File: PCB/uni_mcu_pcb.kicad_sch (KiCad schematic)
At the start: 1 part

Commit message: Добавлены некоторые компоненты на плату
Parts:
- added J?: USB_C_Receptacle_USB2.0, symbol Connector:USB_C_Receptacle_USB2.0
- added U?: CA56-12EWA, Display_7Segment:CA56-12EWA, symbol Display_Character:CA56-12EWA
- added U?: USBLC6-2P6, Package_TO_SOT_SMD:SOT-666, symbol Power_Protection:USBLC6-2P6
- added U?: CH330N, Package_SO:SOIC-8_3.9x4.9mm_P1.27mm, symbol Interface_USB:CH330N
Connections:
- new net: J?.A1 (GND), J?.A12 (GND), J?.B1 (GND), J?.B12 (GND)
- new net: J?.A4 (VBUS), J?.A9 (VBUS), J?.B4 (VBUS), J?.B9 (VBUS)
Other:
- moved on the sheet: U?
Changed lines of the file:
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@@
 (kicad_sch (version 20211123) (generator eeschema)
   (paper "A4")
-  (symbol (lib_id "MCU_ST_STM32F0:STM32F030C8Tx") (at 113.03 88.9 0) (unit 1)
+  (symbol (lib_id "Connector:USB_C_Receptacle_USB2.0") (at 29.845 62.23 0) (unit 1)
     (in_bom yes) (on_board yes) (fields_autoplaced)
-    (property "Reference" "U?" (id 0) (at 117.5894 129.0304 0)
+    (property "Reference" "J?" (id 0) (at 29.845 40.7502 0))
+    (property "Value" "USB_C_Receptacle_USB2.0" (id 1) (at 29.845 43.2871 0))
+    (property "Footprint" "" (id 2) (at 33.655 62.23 0)
+      (effects (font (size 1.27 1.27)) hide)
+    )
+    (property "Datasheet" "https://www.usb.org/sites/default/files/documents/usb_type-c.zip" (id 3) (at 33.655 62.23 0)
+      (effects (font (size 1.27 1.27)) hide)
+    )
+    (pin "A1")
+    (pin "A12")
+    (pin "A4")
+    (pin "A5")
+    (pin "A6")
+    (pin "A7")
+    (pin "A8")
+    (pin "A9")
+    (pin "B1")
+    (pin "B12")
+    (pin "B4")
+    (pin "B5")
+    (pin "B6")
+    (pin "B7")
+    (pin "B8")
+    (pin "B9")
+    (pin "S1")
+  )
+  (symbol (lib_id "Display_Character:CA56-12EWA") (at 232.41 65.405 0) (unit 1)
+    (in_bom yes) (on_board yes) (fields_autoplaced)
+    (property "Reference" "U?" (id 0) (at 232.41 49.0052 0))
+    (property "Value" "CA56-12EWA" (id 1) (at 232.41 51.5421 0))
+    (property "Footprint" "Display_7Segment:CA56-12EWA" (id 2) (at 232.41 80.645 0)
+      (effects (font (size 1.27 1.27)) hide)
+    )
+    (property "Datasheet" "http://www.kingbrightusa.com/images/catalog/SPEC/CA56-12EWA.pdf" (id 3) (at 221.488 64.643 0)
+      (effects (font (size 1.27 1.27)) hide)
+    )
+    (pin "1")
+    (pin "10")
+    (pin "11")
+    (pin "12")
+    (pin "2")
+    (pin "3")
+    (pin "4")
+    (pin "5")
+    (pin "6")
+    (pin "7")
+    (pin "8")
+    (pin "9")
+  )
+  (symbol (lib_id "Power_Protection:USBLC6-2P6") (at 67.31 57.785 0) (unit 1)
+    (in_bom yes) (on_board yes) (fields_autoplaced)
+    (property "Reference" "U?" (id 0) (at 70.0787 46.4652 0)
       (effects (font (size 1.27 1.27)) (justify left))
     )
-    (property "Value" "STM32F030C8Tx" (id 1) (at 117.5894 131.5673 0)
+    (property "Value" "USBLC6-2P6" (id 1) (at 70.0787 49.0021 0)
       (effects (font (size 1.27 1.27)) (justify left))
     )
-    (property "Footprint" "Package_QFP:LQFP-48_7x7mm_P0.5mm" (id 2) (at 100.33 127 0)
+    (property "Footprint" "Package_TO_SOT_SMD:SOT-666" (id 2) (at 67.31 70.485 0)
+      (effects (font (size 1.27 1.27)) hide)
+    )
+    (property "Datasheet" "https://www.st.com/resource/en/datasheet/usblc6-2.pdf" (id 3) (at 72.39 48.895 0)
+      (effects (font (size 1.27 1.27)) hide)
+    )
+    (pin "1")
+    (pin "2")
+    (pin "3")
+    (pin "4")
+    (pin "5")
+    (pin "6")
+  )
+  (symbol (lib_id "Interface_USB:CH330N") (at 99.695 60.325 0) (unit 1)
+    (in_bom yes) (on_board yes) (fields_autoplaced)
+    (property "Reference" "U?" (id 0) (at 101.7144 51.5452 0)
+      (effects (font (size 1.27 1.27)) (justify left))
+    )
+    (property "Value" "CH330N" (id 1) (at 101.7144 54.0821 0)
+      (effects (font (size 1.27 1.27)) (justify left))
+    )
+    (property "Footprint" "Package_SO:SOIC-8_3.9x4.9mm_P1.27mm" (id 2) (at 95.885 41.275 0)
+      (effects (font (size 1.27 1.27)) hide)
+    )
+    (property "Datasheet" "http://www.wch.cn/downloads/file/240.html" (id 3) (at 97.155 55.245 0)
+      (effects (font (size 1.27 1.27)) hide)
+    )
+    (pin "1")
+    (pin "2")
+    (pin "3")
+    (pin "4")
+    (pin "5")
+    (pin "6")
+    (pin "7")
+    (pin "8")
+  )
+  (symbol (lib_id "MCU_ST_STM32F0:STM32F030C8Tx") (at 144.78 105.41 0) (unit 1)
+    (in_bom yes) (on_board yes) (fields_autoplaced)
+    (property "Reference" "U?" (id 0) (at 149.3394 145.5404 0)
+      (effects (font (size 1.27 1.27)) (justify left))
+    )
+    (property "Value" "STM32F030C8Tx" (id 1) (at 149.3394 148.0773 0)
+      (effects (font (size 1.27 1.27)) (justify left))
+    )
+    (property "Footprint" "Package_QFP:LQFP-48_7x7mm_P0.5mm" (id 2) (at 132.08 143.51 0)
       (effects (font (size 1.27 1.27)) (justify right) hide)
     )
-    (property "Datasheet" "http://www.st.com/st-web-ui/static/active/en/resource/technical/document/datasheet/DM00088500.pdf" (id 3) (at 113.03 88.9 0)
+    (property "Datasheet" "http://www.st.com/st-web-ui/static/active/en/resource/technical/document/datasheet/DM00088500.pdf" (id 3) (at 144.78 105.41 0)
       (effects (font (size 1.27 1.27)) hide)
     )
@@
   )
   (symbol_instances
+    (path "/07a403f1-6381-4bd2-8292-ac2034cbc455"
+      (reference "J?") (unit 1) (value "USB_C_Receptacle_USB2.0") (footprint "")
+    )
+    (path "/0a12c89a-af2f-470d-8dce-82d7660071a7"
+      (reference "U?") (unit 1) (value "CA56-12EWA") (footprint "Display_7Segment:CA56-12EWA")
+    )
+    (path "/53f63d0e-ec90-45fe-9dc8-f6cd54e6da9b"
+      (reference "U?") (unit 1) (value "USBLC6-2P6") (footprint "Package_TO_SOT_SMD:SOT-666")
+    )
+    (path "/73d50e38-29fc-4c84-a7fe-f3c205911e63"
+      (reference "U?") (unit 1) (value "CH330N") (footprint "Package_SO:SOIC-8_3.9x4.9mm_P1.27mm")
+    )
     (path "/94fd8e77-4a43-4779-a00d-e9f140b3d12f"
       (reference "U?") (unit 1) (value "STM32F030C8Tx") (footprint "Package_QFP:LQFP-48_7x7mm_P0.5mm")

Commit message: Схемотехника разработана на 80%
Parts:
- removed U?: CA56-12EWA, Display_7Segment:CA56-12EWA, symbol Display_Character:CA56-12EWA
- added C? (x8): C, symbol Device:C
- added D?: LED_BGRK, symbol Device:LED_BGRK
- added D?: D_TVS, symbol Device:D_TVS
- added D? (x2): DIODE, symbol Simulation_SPICE:DIODE
- added J?: Conn_02x06_Odd_Even, symbol Connector_Generic:Conn_02x06_Odd_Even
- added Q? (x4): Q_NPN_BCE, symbol Device:Q_NPN_BCE
- added R? (x15): R, symbol Device:R
- added SW? (x2): SW_DIP_x01, symbol Switch:SW_DIP_x01
- added U?: LD1117S33TR_SOT223, Package_TO_SOT_SMD:SOT-223-3_TabPin2, symbol Regulator_Linear:LD1117S33TR_SOT223
- added U?: W25Q32JVSS, Package_SO:SOIC-8_5.23x5.23mm_P1.27mm, symbol Memory_Flash:W25Q32JVSS
- added U?: CC56-12CGKWA, Display_7Segment:CA56-12CGKWA, symbol Display_Character:CC56-12CGKWA
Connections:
- net GND: now reaches J?.A1 (GND), J?.A12 (GND), J?.B1 (GND), J?.B12 (GND)
- net GND: now also J?.S1 (SHIELD), U?.2 (GND), U?.23 (VSS), U?.3 (GND), U?.47 (VSS), U?.8 (VSSA), C?.1, C?.2, C?.2, C?.2, C?.2, C?.2, C?.2, C?.2, D?.1 (A1), D?.4 (K), J?.11 (Pin_11), Q?.3 (E), Q?.3 (E), Q?.3 (E), Q?.3 (E), R?.1, R?.2, R?.2, SW?.1, SW?.1, U?.1 (GND), U?.4 (GND)
- net +5V: now reaches J?.A4 (VBUS), J?.A9 (VBUS), J?.B4 (VBUS), J?.B9 (VBUS)
- net +5V: now also U?.5 (VBUS), U?.5 (VCC), C?.1, D?.1 (A), J?.12 (Pin_12)
- net CC1: now reaches J?.A5 (CC1)
- net CC1: now also R?.1
- net USB_D+: now reaches J?.A6 (D+)
- net USB_D+: now also J?.B6 (D+), R?.1
- net USB_D-: now reaches J?.A7 (D-)
- net USB_D-: now also J?.B7 (D-), R?.1
- net CC2: now reaches J?.B5 (CC2)
- net CC2: now also R?.1
- net at U?.1 (I/O1): now also U?.2 (UD-), U?.6 (I/O1), R?.2
- net at U?.3 (I/O2): now also U?.1 (UD+), U?.4 (I/O2), R?.2
- net USART1_RX: now reaches U?.6 (TXD)
- net USART1_RX: now also U?.43 (PB7)
- net USART1_TX: now reaches U?.7 (RXD)
- net USART1_TX: now also U?.42 (PB6)
- net at U?.8 (V3): now also C?.2
- net +3V3: now reaches U?.1 (VDD)
- net +3V3: now also U?.24 (VDD), U?.48 (VDD), U?.9 (VDDA), C?.1, C?.1, C?.1, C?.1, C?.1, J?.10 (Pin_10), R?.1, R?.2, R?.2, U?.2 (VO), U?.8 (VCC)
- net CA1_CTRL: now reaches U?.10 (PA0)
- net CA1_CTRL: now also R?.1
- net CA2_CTRL: now reaches U?.11 (PA1)
- net CA2_CTRL: now also R?.1
- net USART2_TX: now reaches U?.12 (PA2)
- net USART2_TX: now also J?.6 (Pin_6)
- net USART2_RX: now reaches U?.13 (PA3)
- net USART2_RX: now also J?.8 (Pin_8)
- net CA3_CTRL: now reaches U?.14 (PA4)
- net CA3_CTRL: now also R?.1
- net CA4_CTRL: now reaches U?.15 (PA5)
- net CA4_CTRL: now also R?.1
- net a: now reaches U?.16 (PA6)
- net a: now also U?.11 (a)
- net b: now reaches U?.17 (PA7)
- net b: now also U?.7 (b)
- net PB0_IO: now reaches U?.18 (PB0)
- net PB0_IO: now also J?.1 (Pin_1)
- net PB1_IO: now reaches U?.19 (PB1)
- net PB1_IO: now also J?.3 (Pin_3)
- net at U?.2 (PC13): now also R?.2
- net FLASH_CS: now reaches U?.20 (PB2)
- net FLASH_CS: now also U?.1 (~{CS})
- net SW1: now reaches U?.21 (PB10)
- net SW1: now also R?.1, SW?.2
- net SW2: now reaches U?.22 (PB11)
- net SW2: now also R?.1, SW?.2
- net c: now reaches U?.29 (PA8)
- net c: now also U?.4 (c)
- net at U?.3 (PC14): now also R?.2
- net d: now reaches U?.30 (PA9)
- net d: now also U?.2 (d)
- net e: now reaches U?.31 (PA10)
- net e: now also U?.1 (e)
- net f: now reaches U?.32 (PA11)
- net f: now also U?.10 (f)
- net g: now reaches U?.33 (PA12)
- net g: now also U?.5 (g)
- net dpx_swdio: now reaches U?.34 (PA13)
- net swclk: now reaches U?.37 (PA14)
- net SPI1_SCK: now reaches U?.39 (PB3)
- net SPI1_SCK: now also J?.5 (Pin_5), U?.6 (CLK)
- net at U?.4 (PC15): now also R?.2
- net SPI1_MISO: now reaches U?.40 (PB4)
- net SPI1_MISO: now also J?.7 (Pin_7), U?.2 (DO(IO1))
- net SPI1_MOSI: now reaches U?.41 (PB5)
- net SPI1_MOSI: now also J?.9 (Pin_9), U?.5 (DI(IO0))
- net at U?.44 (BOOT0): now also R?.2
- net I2C1_SDA: now reaches U?.45 (PB8)
- net I2C1_SDA: now also J?.2 (Pin_2)
- net I2C1_SCL: now reaches U?.46 (PB9)
- net I2C1_SCL: now also J?.4 (Pin_4)
- net RESET: now reaches U?.7 (NRST)
- net RESET: now also U?.7 (IO3)
- new net: D?.3 (RA), R?.1
- new net: C?.1, D?.2 (K), D?.2 (K), U?.3 (VI)
- new net: D?.2 (GA), R?.1
- new net: Q?.1 (B), R?.2 (x4)
- new net: D?.1 (BA), R?.1
- new net: R?.2, U?.3 (IO2)
- new net +BATT: D?.1 (A), D?.2 (A2)
- new net CA1: Q?.2 (C), U?.12 (CC1)
- new net CA2: Q?.2 (C), U?.9 (CC2)
- new net CA3: Q?.2 (C), U?.8 (CC3)
- new net CA4: Q?.2 (C), U?.6 (CC4)
- new net dpx: U?.3 (DPX)
- no-connect marks 0 -> 1
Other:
- moved on the sheet: U?

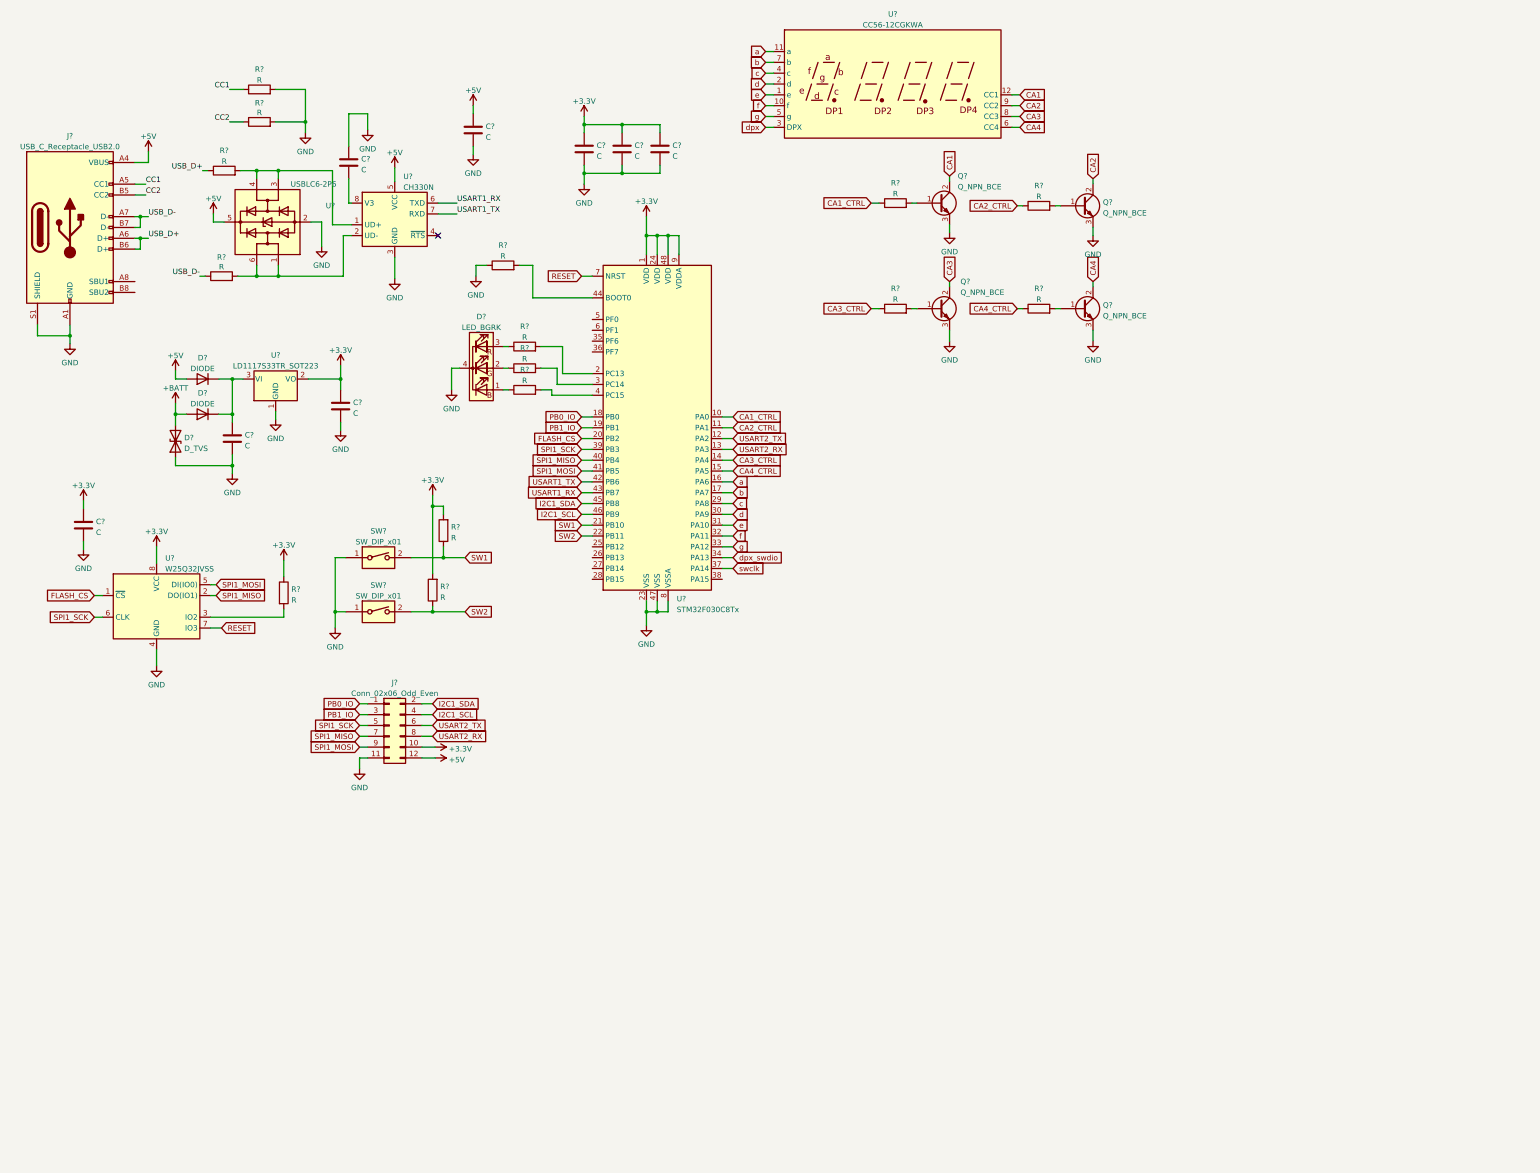
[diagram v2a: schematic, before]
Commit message: Добавлено управление нагрузкой
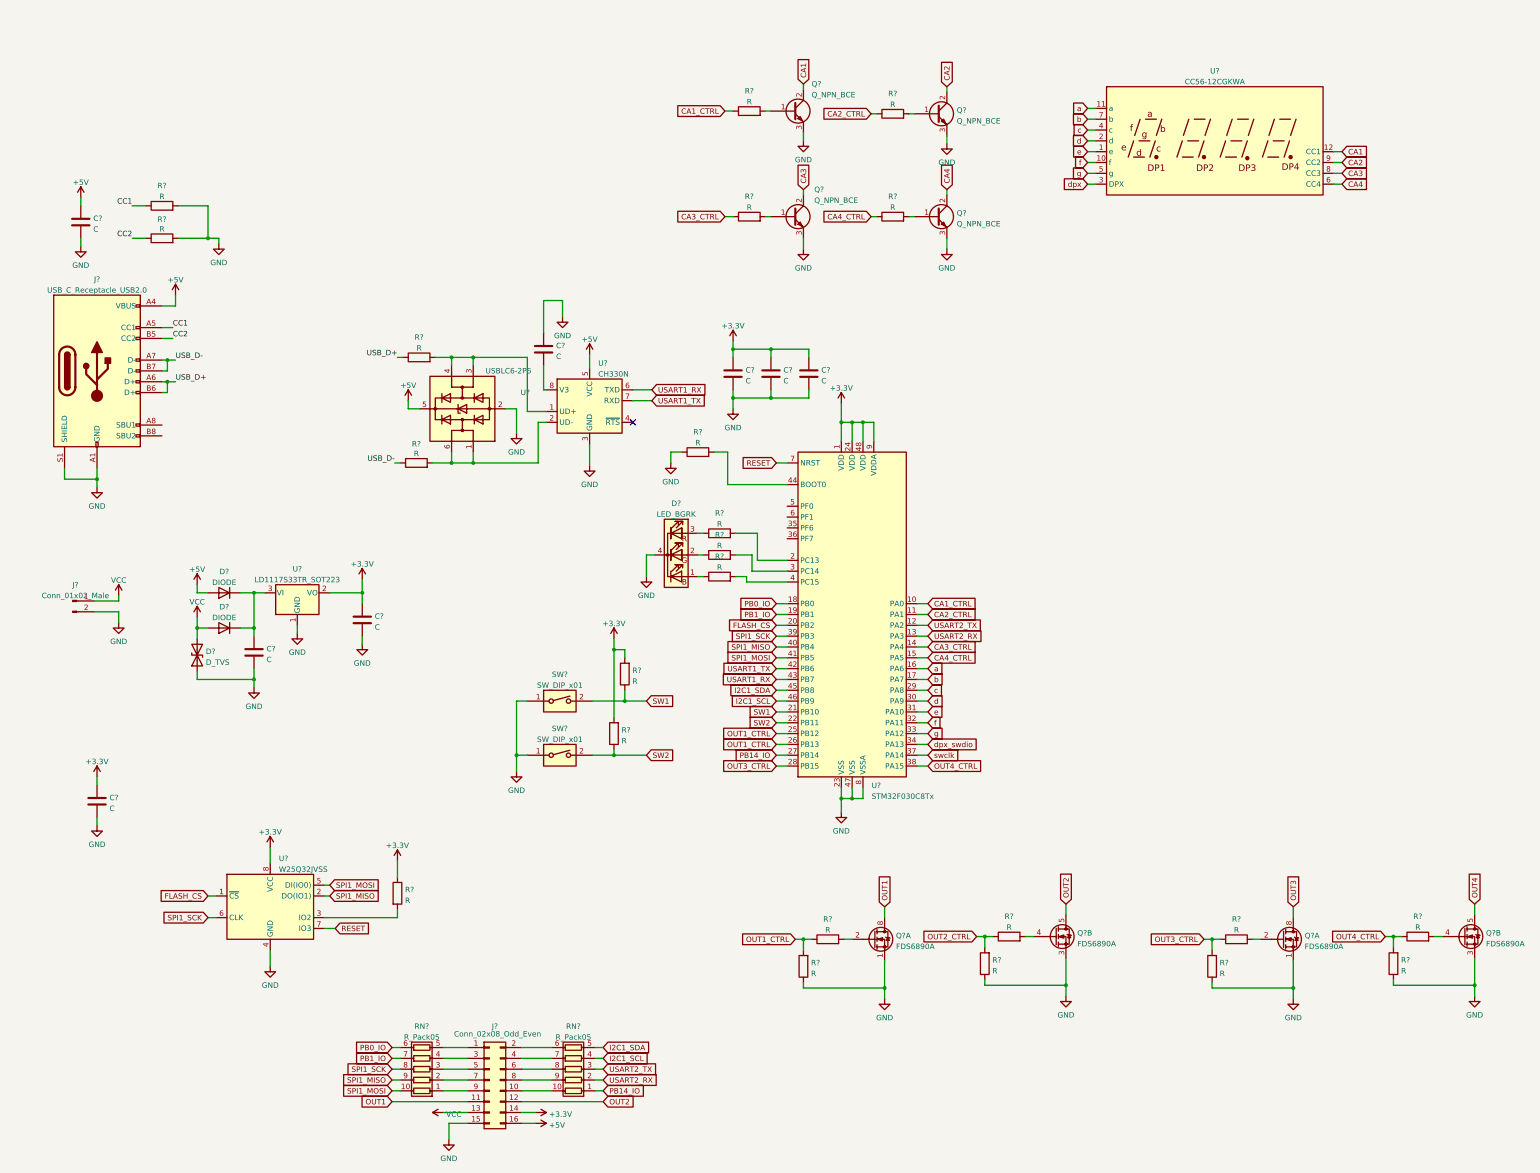
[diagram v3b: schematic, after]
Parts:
- removed J?: Conn_02x06_Odd_Even, symbol Connector_Generic:Conn_02x06_Odd_Even
- added J?: Conn_02x08_Odd_Even, symbol Connector_Generic:Conn_02x08_Odd_Even
- added J?: Conn_01x02_Male, symbol Connector:Conn_01x02_Male
- added Q? (x4): FDS6890A, Package_SO:SOIC-8_3.9x4.9mm_P1.27mm, symbol Transistor_FET:FDS6890A
- added R? (x8): R, symbol Device:R
- added RN? (x2): R_Pack05, symbol Device:R_Pack05
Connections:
- net +3V3: now also J?.14 (Pin_14)
- net +5V: now also J?.16 (Pin_16)
- net GND: now also J?.15 (Pin_15), J?.2 (Pin_2), Q?.1 (S1), Q?.1 (S1), Q?.3 (S2), Q?.3 (S2), R?.1, R?.1, R?.1, R?.1
- net I2C1_SCL: now also RN?.4 (R4.1)
- net I2C1_SDA: now also RN?.5 (R5.1)
- net PB0_IO: now also RN?.6 (R5.2)
- net PB1_IO: now also RN?.7 (R4.2)
- net SPI1_MISO: now also RN?.9 (R2.2)
- net SPI1_MOSI: now also RN?.10 (R1.2)
- net SPI1_SCK: now also RN?.8 (R3.2)
- net USART2_RX: now also RN?.2 (R2.1)
- net USART2_TX: now also RN?.3 (R3.1)
- net OUT1_CTRL: now reaches U?.25 (PB12)
- net OUT1_CTRL: now also U?.26 (PB13), R?.1, R?.2
- net PB14_IO: now reaches U?.27 (PB14)
- net PB14_IO: now also RN?.1 (R1.1)
- net OUT3_CTRL: now reaches U?.28 (PB15)
- net OUT3_CTRL: now also R?.1, R?.2
- net OUT4_CTRL: now reaches U?.38 (PA15)
- net OUT4_CTRL: now also R?.1, R?.2
- net +BATT renamed VCC
- net VCC: now also J?.1 (Pin_1), J?.13 (Pin_13)
- new net: J?.9 (Pin_9), RN?.1 (R1.1)
- new net: J?.7 (Pin_7), RN?.2 (R2.1)
- new net: J?.5 (Pin_5), RN?.3 (R3.1)
- new net: J?.3 (Pin_3), RN?.4 (R4.1)
- new net: J?.1 (Pin_1), RN?.5 (R5.1)
- new net: Q?.2 (G1), R?.2 (x2)
- new net: Q?.4 (G2), R?.2 (x2)
- new net: J?.10 (Pin_10), RN?.10 (R1.2)
- new net: J?.2 (Pin_2), RN?.6 (R5.2)
- new net: J?.4 (Pin_4), RN?.7 (R4.2)
- new net: J?.6 (Pin_6), RN?.8 (R3.2)
- new net: J?.8 (Pin_8), RN?.9 (R2.2)
- new net OUT1: J?.11 (Pin_11), Q?.7 (D1), Q?.8 (D1)
- new net OUT2: J?.12 (Pin_12), Q?.5 (D2), Q?.6 (D2)
- new net OUT2_CTRL: R?.1, R?.2
- new net OUT3: Q?.7 (D1), Q?.8 (D1)
- new net OUT4: Q?.5 (D2), Q?.6 (D2)
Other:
- moved on the sheet: C?, D?, J?, Q?, R?, SW?, U?
